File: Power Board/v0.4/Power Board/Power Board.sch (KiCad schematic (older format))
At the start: 26 parts, among them J1 Battery In, J2 JST B2PS-VH, J3 JST B2PS-VH, J4 JST B2PS-VH, J5 JST B2PS-VH, J6 JST B2PS-VH, J7 JST B2PS-VH, J9 Raspberry Pi, SW1 SW_Push

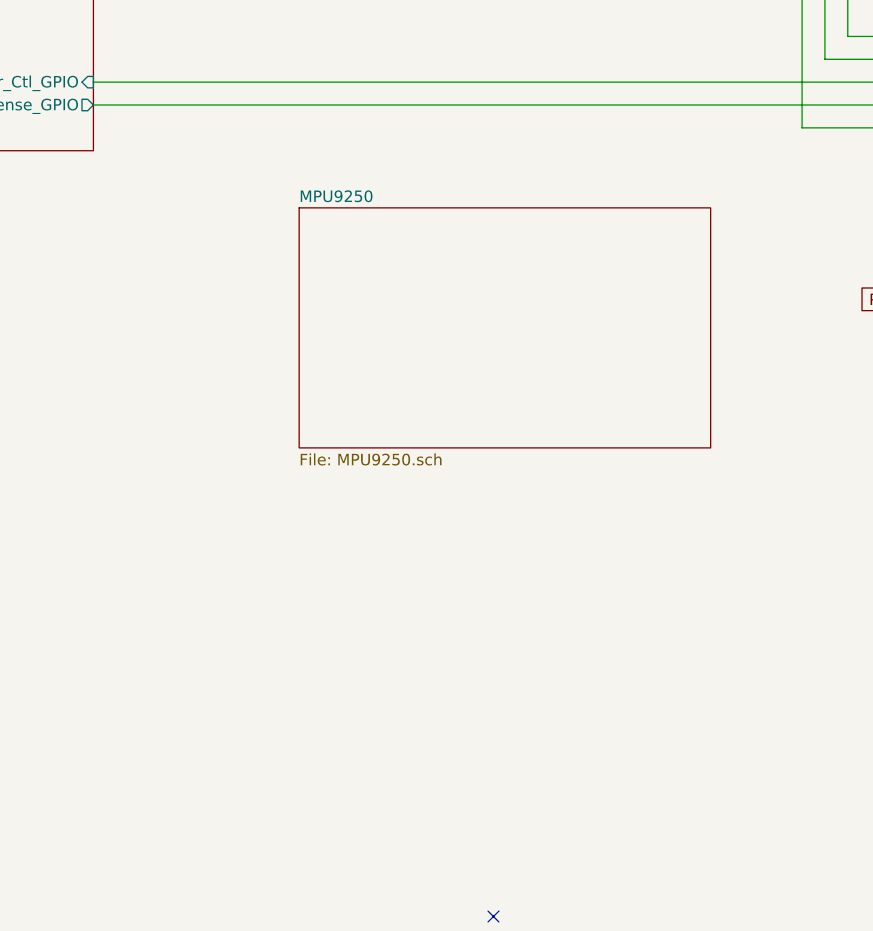
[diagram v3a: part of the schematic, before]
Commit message: Add ADC to monitor battery voltage.
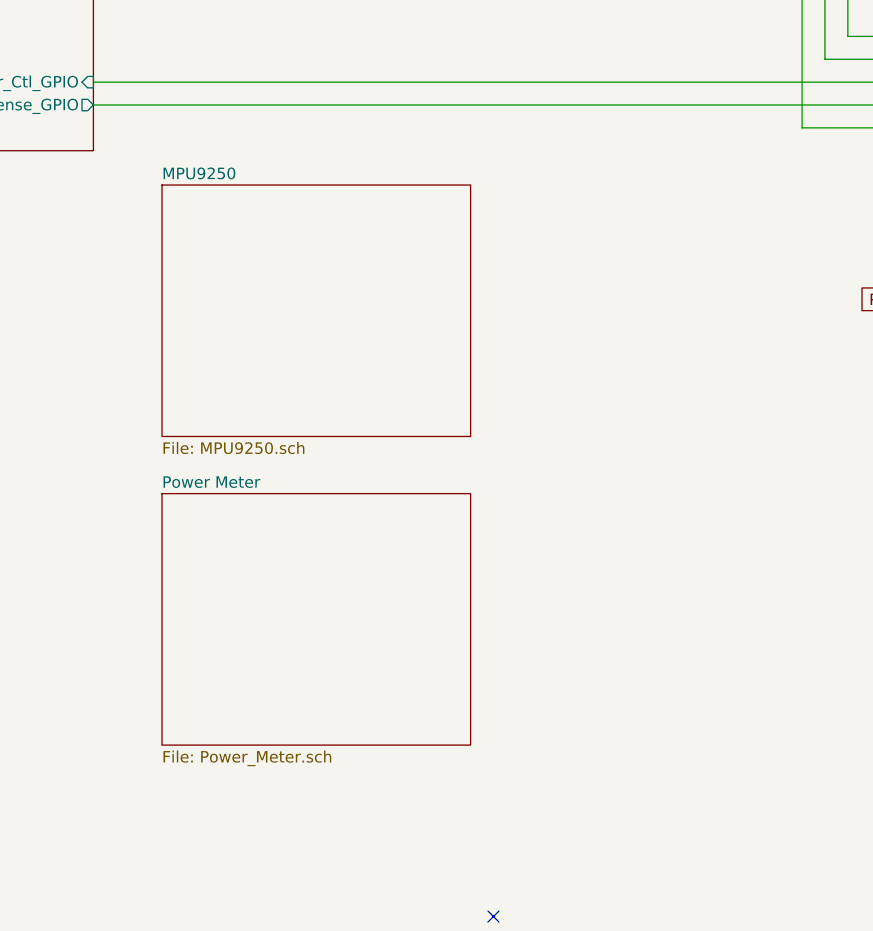
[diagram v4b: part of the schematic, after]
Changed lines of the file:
@@
 $Descr USLetter 11000 8500
 encoding utf-8
-Sheet 1 4
+Sheet 1 5
 Title "LED Cube Power Board"
 Date ""
@@
 $EndComp
 $Sheet
-S 5000 5250 1800 1050
+S 4400 5150 1350 1100
 U 5CBBBF0A
 F0 "MPU9250" 50
@@
 Wire Wire Line
 	7900 5650 8500 5650
+$Sheet
+S 4400 6500 1350 1100
+U 5CB541CC
+F0 "Power Meter" 50
+F1 "Power_Meter.sch" 50
+$EndSheet
 $EndSCHEMATC

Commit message: Almost Rough Draft Done
Mostly routed but needs lots of TLC. Need to check rule definitions before DRC
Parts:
- added R24: 100k, Resistor_SMD:R_0603_1608Metric, symbol Device:R
- L1, L2, L3, L4, L5, L6: value 70R -> 60R; footprint Inductor_SMD:L_0603_1608Metric -> Inductor_SMD:L_1206_3216Metric; Digikey No. 490-5224-1-ND -> 587-1770-1-ND; Manufacturer Murata -> Taiyo Yuden; Part No. BLM18SG700TN1D -> FBMJ3216HM600-T
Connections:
- wire segments 88 -> 89
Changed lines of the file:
@@
 $EndSheet
 Wire Wire Line
-	4900 4300 4900 2300
+	4900 4300 4900 3400
 Text Label 8850 4300 2    50   ~ 0
 +5.2V
@@
 	8300 3400 8200 3400
 $Comp
-L Device:L_Core_Ferrite_Small L6
-U 1 1 5CA7F909
-P 8400 3400
-F 0 "L6" V 8605 3400 50  0000 C CNN
-F 1 "70R" V 8514 3400 50  0000 C CNN
-F 2 "Inductor_SMD:L_0603_1608Metric" H 8400 3400 50  0001 C CNN
-F 3 "~" H 8400 3400 50  0001 C CNN
-F 4 "490-5224-1-ND" H 0   0   50  0001 C CNN "Digikey No."
-F 5 "Murata" H 0   0   50  0001 C CNN "Manufacturer"
-F 6 " BLM18SG700TN1D " H 0   0   50  0001 C CNN "Part No."
-	1    8400 3400
-	0    -1   -1   0
-$EndComp
-$Comp
-L Device:L_Core_Ferrite_Small L5
-U 1 1 5CA7EB66
-P 8400 3100
-F 0 "L5" V 8605 3100 50  0000 C CNN
-F 1 "70R" V 8514 3100 50  0000 C CNN
-F 2 "Inductor_SMD:L_0603_1608Metric" H 8400 3100 50  0001 C CNN
-F 3 "~" H 8400 3100 50  0001 C CNN
-F 4 "490-5224-1-ND" H 0   0   50  0001 C CNN "Digikey No."
-F 5 "Murata" H 0   0   50  0001 C CNN "Manufacturer"
-F 6 " BLM18SG700TN1D " H 0   0   50  0001 C CNN "Part No."
-	1    8400 3100
-	0    -1   -1   0
-$EndComp
-$Comp
-L Device:L_Core_Ferrite_Small L4
-U 1 1 5CA7DCF6
-P 8400 2800
-F 0 "L4" V 8605 2800 50  0000 C CNN
-F 1 "70R" V 8514 2800 50  0000 C CNN
-F 2 "Inductor_SMD:L_0603_1608Metric" H 8400 2800 50  0001 C CNN
-F 3 "~" H 8400 2800 50  0001 C CNN
-F 4 "490-5224-1-ND" H 0   0   50  0001 C CNN "Digikey No."
-F 5 "Murata" H 0   0   50  0001 C CNN "Manufacturer"
-F 6 " BLM18SG700TN1D " H 0   0   50  0001 C CNN "Part No."
-	1    8400 2800
-	0    -1   -1   0
-$EndComp
-$Comp
-L Device:L_Core_Ferrite_Small L3
-U 1 1 5CA7CC63
-P 8400 2500
-F 0 "L3" V 8605 2500 50  0000 C CNN
-F 1 "70R" V 8514 2500 50  0000 C CNN
-F 2 "Inductor_SMD:L_0603_1608Metric" H 8400 2500 50  0001 C CNN
-F 3 "~" H 8400 2500 50  0001 C CNN
-F 4 "490-5224-1-ND" H 0   0   50  0001 C CNN "Digikey No."
-F 5 "Murata" H 0   0   50  0001 C CNN "Manufacturer"
-F 6 " BLM18SG700TN1D " H 0   0   50  0001 C CNN "Part No."
-	1    8400 2500
-	0    -1   -1   0
-$EndComp
-$Comp
-L Device:L_Core_Ferrite_Small L2
-U 1 1 5CA7B064
-P 8400 2200
-F 0 "L2" V 8605 2200 50  0000 C CNN
-F 1 "70R" V 8514 2200 50  0000 C CNN
-F 2 "Inductor_SMD:L_0603_1608Metric" H 8400 2200 50  0001 C CNN
-F 3 "~" H 8400 2200 50  0001 C CNN
-F 4 "490-5224-1-ND" H 0   0   50  0001 C CNN "Digikey No."
-F 5 "Murata" H 0   0   50  0001 C CNN "Manufacturer"
-F 6 " BLM18SG700TN1D " H 0   0   50  0001 C CNN "Part No."
-	1    8400 2200
-	0    -1   -1   0
-$EndComp
-$Comp
 L Device:L_Core_Ferrite_Small L1
 U 1 1 5CA6BA0E
 P 8400 1900
 F 0 "L1" V 8605 1900 50  0000 C CNN
-F 1 "70R" V 8514 1900 50  0000 C CNN
-F 2 "Inductor_SMD:L_0603_1608Metric" H 8400 1900 50  0001 C CNN
-F 3 "~" H 8400 1900 50  0001 C CNN
-F 4 "490-5224-1-ND" H 0   0   50  0001 C CNN "Digikey No."
-F 5 "Murata" H 0   0   50  0001 C CNN "Manufacturer"
-F 6 " BLM18SG700TN1D " H 0   0   50  0001 C CNN "Part No."
+F 1 "60R" V 8514 1900 50  0000 C CNN
+F 2 "Inductor_SMD:L_1206_3216Metric" H 8400 1900 50  0001 C CNN
+F 3 "https://ds.yuden.co.jp/TYCOMPAS/ut/detail?pn=FBMJ3216HM600-T%20%20&u=M" H 8400 1900 50  0001 C CNN
+F 4 "587-1770-1-ND" H 0   0   50  0001 C CNN "Digikey No."
+F 5 "Taiyo Yuden" H 0   0   50  0001 C CNN "Manufacturer"
+F 6 "FBMJ3216HM600-T" H 0   0   50  0001 C CNN "Part No."
 	1    8400 1900
 	0    -1   -1   0
@@
 F1 "Power_Meter.sch" 50
 $EndSheet
+$Comp
+L Device:R R24
+U 1 1 5CC09EBC
+P 4900 3250
+F 0 "R24" H 4970 3296 50  0000 L CNN
+F 1 "100k" H 4970 3205 50  0000 L CNN
+F 2 "Resistor_SMD:R_0603_1608Metric" V 4830 3250 50  0001 C CNN
+F 3 "~" H 4900 3250 50  0001 C CNN
+	1    4900 3250
+	1    0    0    -1
+$EndComp
+Wire Wire Line
+	4900 3100 4900 2300
+$Comp
+L Device:L_Core_Ferrite_Small L2
+U 1 1 5CC32C1C
+P 8400 2200
+F 0 "L2" V 8605 2200 50  0000 C CNN
+F 1 "60R" V 8514 2200 50  0000 C CNN
+F 2 "Inductor_SMD:L_1206_3216Metric" H 8400 2200 50  0001 C CNN
+F 3 "https://ds.yuden.co.jp/TYCOMPAS/ut/detail?pn=FBMJ3216HM600-T%20%20&u=M" H 8400 2200 50  0001 C CNN
+F 4 "587-1770-1-ND" H 0   300 50  0001 C CNN "Digikey No."
+F 5 "Taiyo Yuden" H 0   300 50  0001 C CNN "Manufacturer"
+F 6 "FBMJ3216HM600-T" H 0   300 50  0001 C CNN "Part No."
+	1    8400 2200
+	0    -1   -1   0
+$EndComp
+$Comp
+L Device:L_Core_Ferrite_Small L3
+U 1 1 5CC3439F
+P 8400 2500
+F 0 "L3" V 8605 2500 50  0000 C CNN
+F 1 "60R" V 8514 2500 50  0000 C CNN
+F 2 "Inductor_SMD:L_1206_3216Metric" H 8400 2500 50  0001 C CNN
+F 3 "https://ds.yuden.co.jp/TYCOMPAS/ut/detail?pn=FBMJ3216HM600-T%20%20&u=M" H 8400 2500 50  0001 C CNN
+F 4 "587-1770-1-ND" H 0   600 50  0001 C CNN "Digikey No."
+F 5 "Taiyo Yuden" H 0   600 50  0001 C CNN "Manufacturer"
+F 6 "FBMJ3216HM600-T" H 0   600 50  0001 C CNN "Part No."
+	1    8400 2500
+	0    -1   -1   0
+$EndComp
+$Comp
+L Device:L_Core_Ferrite_Small L4
+U 1 1 5CC356E6
+P 8400 2800
+F 0 "L4" V 8605 2800 50  0000 C CNN
+F 1 "60R" V 8514 2800 50  0000 C CNN
+F 2 "Inductor_SMD:L_1206_3216Metric" H 8400 2800 50  0001 C CNN
+F 3 "https://ds.yuden.co.jp/TYCOMPAS/ut/detail?pn=FBMJ3216HM600-T%20%20&u=M" H 8400 2800 50  0001 C CNN
+F 4 "587-1770-1-ND" H 0   900 50  0001 C CNN "Digikey No."
+F 5 "Taiyo Yuden" H 0   900 50  0001 C CNN "Manufacturer"
+F 6 "FBMJ3216HM600-T" H 0   900 50  0001 C CNN "Part No."
+	1    8400 2800
+	0    -1   -1   0
+$EndComp
+$Comp
+L Device:L_Core_Ferrite_Small L5
+U 1 1 5CC3696C
+P 8400 3100
+F 0 "L5" V 8605 3100 50  0000 C CNN
+F 1 "60R" V 8514 3100 50  0000 C CNN
+F 2 "Inductor_SMD:L_1206_3216Metric" H 8400 3100 50  0001 C CNN
+F 3 "https://ds.yuden.co.jp/TYCOMPAS/ut/detail?pn=FBMJ3216HM600-T%20%20&u=M" H 8400 3100 50  0001 C CNN
+F 4 "587-1770-1-ND" H 0   1200 50  0001 C CNN "Digikey No."
+F 5 "Taiyo Yuden" H 0   1200 50  0001 C CNN "Manufacturer"
+F 6 "FBMJ3216HM600-T" H 0   1200 50  0001 C CNN "Part No."
+	1    8400 3100
+	0    -1   -1   0
+$EndComp
+$Comp
+L Device:L_Core_Ferrite_Small L6
+U 1 1 5CC38C63
+P 8400 3400
+F 0 "L6" V 8605 3400 50  0000 C CNN
+F 1 "60R" V 8514 3400 50  0000 C CNN
+F 2 "Inductor_SMD:L_1206_3216Metric" H 8400 3400 50  0001 C CNN
+F 3 "https://ds.yuden.co.jp/TYCOMPAS/ut/detail?pn=FBMJ3216HM600-T%20%20&u=M" H 8400 3400 50  0001 C CNN
+F 4 "587-1770-1-ND" H 0   1500 50  0001 C CNN "Digikey No."
+F 5 "Taiyo Yuden" H 0   1500 50  0001 C CNN "Manufacturer"
+F 6 "FBMJ3216HM600-T" H 0   1500 50  0001 C CNN "Part No."
+	1    8400 3400
+	0    -1   -1   0
+$EndComp
 $EndSCHEMATC

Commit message: More routing and zone placements. Needs more TLC Needs DRC review and fix
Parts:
- L7: value 70R -> 60R; footprint Inductor_SMD:L_0603_1608Metric -> Inductor_SMD:L_1206_3216Metric; Digikey No. 490-5224-1-ND -> 587-1770-1-ND; Manufacturer Murata -> Taiyo Yuden; Part No. BLM18SG700TN1D -> FBMJ3216HM600-T
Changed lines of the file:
@@
-$EndComp
-$Comp
-L Device:L_Core_Ferrite_Small L?
-U 1 1 5CC268DC
-P 8400 4300
-AR Path="/5C958DBD/5CC268DC" Ref="L?"  Part="1"
-AR Path="/5CC268DC" Ref="L7"  Part="1"
-F 0 "L7" V 8600 4300 50  0000 C CNN
-F 1 "70R" V 8500 4300 50  0000 C CNN
-F 2 "Inductor_SMD:L_0603_1608Metric" H 8400 4300 50  0001 C CNN
-F 3 "~" H 8400 4300 50  0001 C CNN
-F 4 "Murata" H 1150 1350 50  0001 C CNN "Manufacturer"
-F 5 " BLM18SG700TN1D " H 1150 1350 50  0001 C CNN "Part No."
-F 6 "490-5224-1-ND" H 400 0   50  0001 C CNN "Digikey No."
-	1    8400 4300
-	0    -1   -1   0
 $EndComp
 $Comp
@@
 	0    -1   -1   0
 $EndComp
+$Comp
+L Device:L_Core_Ferrite_Small L7
+U 1 1 5CC7E354
+P 8400 4300
+F 0 "L7" V 8605 4300 50  0000 C CNN
+F 1 "60R" V 8514 4300 50  0000 C CNN
+F 2 "Inductor_SMD:L_1206_3216Metric" H 8400 4300 50  0001 C CNN
+F 3 "https://ds.yuden.co.jp/TYCOMPAS/ut/detail?pn=FBMJ3216HM600-T%20%20&u=M" H 8400 4300 50  0001 C CNN
+F 4 "587-1770-1-ND" H 0   2400 50  0001 C CNN "Digikey No."
+F 5 "Taiyo Yuden" H 0   2400 50  0001 C CNN "Manufacturer"
+F 6 "FBMJ3216HM600-T" H 0   2400 50  0001 C CNN "Part No."
+	1    8400 4300
+	0    -1   -1   0
+$EndComp

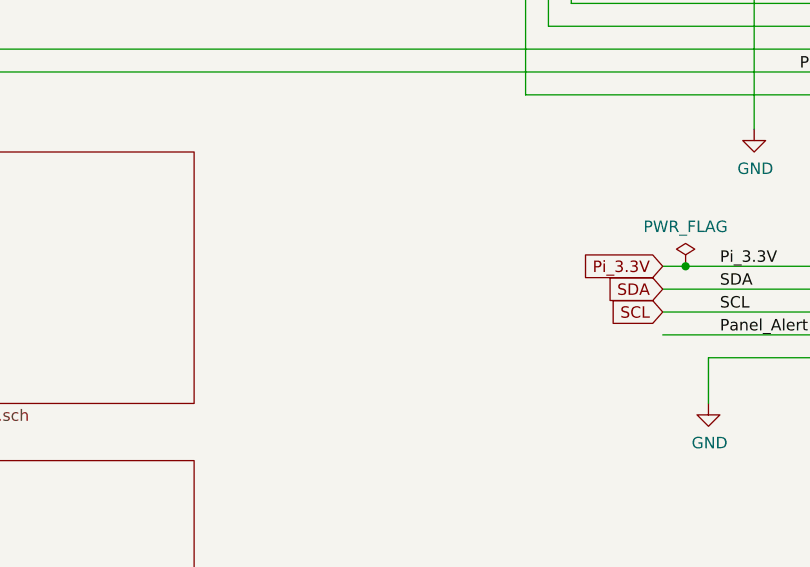
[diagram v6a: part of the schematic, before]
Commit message: Rework routing to panel connectors.  WIP.
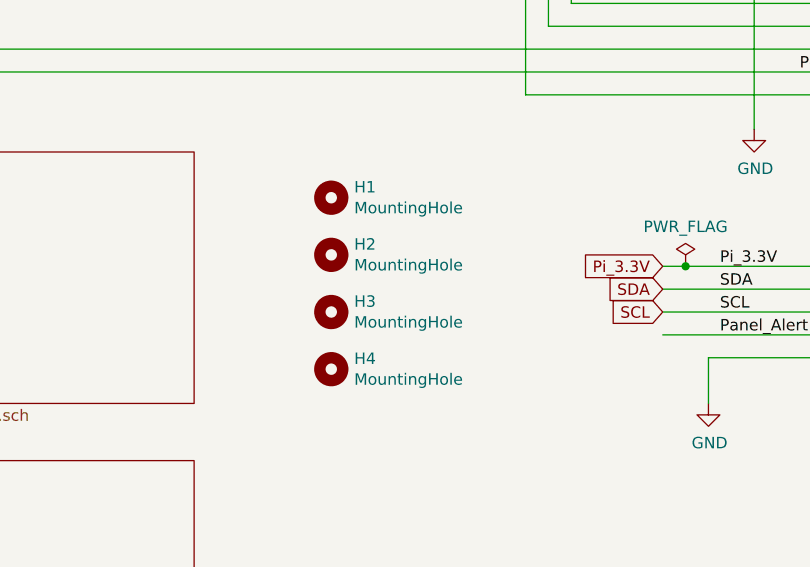
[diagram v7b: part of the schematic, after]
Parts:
- added H1, H2, H3, H4: MountingHole, MountingHole:MountingHole_2.7mm_M2.5, symbol Mechanical:MountingHole
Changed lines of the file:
@@
 	0    -1   -1   0
 $EndComp
+$Comp
+L Mechanical:MountingHole H1
+U 1 1 5CBE4232
+P 6350 5350
+F 0 "H1" H 6450 5396 50  0000 L CNN
+F 1 "MountingHole" H 6450 5305 50  0000 L CNN
+F 2 "MountingHole:MountingHole_2.7mm_M2.5" H 6350 5350 50  0001 C CNN
+F 3 "~" H 6350 5350 50  0001 C CNN
+	1    6350 5350
+	1    0    0    -1
+$EndComp
+$Comp
+L Mechanical:MountingHole H2
+U 1 1 5CBE4288
+P 6350 5600
+F 0 "H2" H 6450 5646 50  0000 L CNN
+F 1 "MountingHole" H 6450 5555 50  0000 L CNN
+F 2 "MountingHole:MountingHole_2.7mm_M2.5" H 6350 5600 50  0001 C CNN
+F 3 "~" H 6350 5600 50  0001 C CNN
+	1    6350 5600
+	1    0    0    -1
+$EndComp
+$Comp
+L Mechanical:MountingHole H3
+U 1 1 5CBE430A
+P 6350 5850
+F 0 "H3" H 6450 5896 50  0000 L CNN
+F 1 "MountingHole" H 6450 5805 50  0000 L CNN
+F 2 "MountingHole:MountingHole_2.7mm_M2.5" H 6350 5850 50  0001 C CNN
+F 3 "~" H 6350 5850 50  0001 C CNN
+	1    6350 5850
+	1    0    0    -1
+$EndComp
+$Comp
+L Mechanical:MountingHole H4
+U 1 1 5CBE438C
+P 6350 6100
+F 0 "H4" H 6450 6146 50  0000 L CNN
+F 1 "MountingHole" H 6450 6055 50  0000 L CNN
+F 2 "MountingHole:MountingHole_2.7mm_M2.5" H 6350 6100 50  0001 C CNN
+F 3 "~" H 6350 6100 50  0001 C CNN
+	1    6350 6100
+	1    0    0    -1
+$EndComp
 $EndSCHEMATC

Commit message: Add 3D models for some components.
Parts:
- J1: footprint Connector_JST:JST_VH_B3PS-VH_1x03_P3.96mm_Horizontal -> Power_Board:JST_VH_B3PS-VH_1x03_P3.96mm_Horizontal
- J2, J3, J4, J5, J6, J7: footprint Connector_JST:JST_VH_B2PS-VH_1x02_P3.96mm_Horizontal -> Power_Board:JST_VH_B2PS-VH_1x02_P3.96mm_Horizontal
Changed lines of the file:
@@
 F 0 "J7" H 9130 3392 50  0000 L CNN
 F 1 "JST B2PS-VH" H 9130 3301 50  0000 L CNN
-F 2 "Connector_JST:JST_VH_B2PS-VH_1x02_P3.96mm_Horizontal" H 9050 3400 50  0001 C CNN
+F 2 "Power_Board:JST_VH_B2PS-VH_1x02_P3.96mm_Horizontal" H 9050 3400 50  0001 C CNN
 F 3 "~" H 9050 3400 50  0001 C CNN
 F 4 "455-1648-ND" H -50 1950 50  0001 C CNN "Digikey No."
@@
 F 0 "J6" H 9130 3092 50  0000 L CNN
 F 1 "JST B2PS-VH" H 9130 3001 50  0000 L CNN
-F 2 "Connector_JST:JST_VH_B2PS-VH_1x02_P3.96mm_Horizontal" H 9050 3100 50  0001 C CNN
+F 2 "Power_Board:JST_VH_B2PS-VH_1x02_P3.96mm_Horizontal" H 9050 3100 50  0001 C CNN
 F 3 "~" H 9050 3100 50  0001 C CNN
 F 4 "455-1648-ND" H -50 1650 50  0001 C CNN "Digikey No."
@@
 F 0 "J5" H 9130 2792 50  0000 L CNN
 F 1 "JST B2PS-VH" H 9130 2701 50  0000 L CNN
-F 2 "Connector_JST:JST_VH_B2PS-VH_1x02_P3.96mm_Horizontal" H 9050 2800 50  0001 C CNN
+F 2 "Power_Board:JST_VH_B2PS-VH_1x02_P3.96mm_Horizontal" H 9050 2800 50  0001 C CNN
 F 3 "~" H 9050 2800 50  0001 C CNN
 F 4 "455-1648-ND" H -50 1350 50  0001 C CNN "Digikey No."
@@
 F 0 "J4" H 9130 2492 50  0000 L CNN
 F 1 "JST B2PS-VH" H 9130 2401 50  0000 L CNN
-F 2 "Connector_JST:JST_VH_B2PS-VH_1x02_P3.96mm_Horizontal" H 9050 2500 50  0001 C CNN
+F 2 "Power_Board:JST_VH_B2PS-VH_1x02_P3.96mm_Horizontal" H 9050 2500 50  0001 C CNN
 F 3 "~" H 9050 2500 50  0001 C CNN
 F 4 "455-1648-ND" H -50 1050 50  0001 C CNN "Digikey No."
@@
 F 0 "J3" H 9130 2192 50  0000 L CNN
 F 1 "JST B2PS-VH" H 9130 2101 50  0000 L CNN
-F 2 "Connector_JST:JST_VH_B2PS-VH_1x02_P3.96mm_Horizontal" H 9050 2200 50  0001 C CNN
+F 2 "Power_Board:JST_VH_B2PS-VH_1x02_P3.96mm_Horizontal" H 9050 2200 50  0001 C CNN
 F 3 "~" H 9050 2200 50  0001 C CNN
 F 4 "455-1648-ND" H -50 750 50  0001 C CNN "Digikey No."
@@
 F 0 "J2" H 9130 1892 50  0000 L CNN
 F 1 "JST B2PS-VH" H 9130 1801 50  0000 L CNN
-F 2 "Connector_JST:JST_VH_B2PS-VH_1x02_P3.96mm_Horizontal" H 9050 1900 50  0001 C CNN
+F 2 "Power_Board:JST_VH_B2PS-VH_1x02_P3.96mm_Horizontal" H 9050 1900 50  0001 C CNN
 F 3 "~" H 9050 1900 50  0001 C CNN
 F 4 "455-1648-ND" H -50 450 50  0001 C CNN "Digikey No."
@@
 F 0 "J1" H 992 2185 50  0000 C CNN
 F 1 "Battery In" H 992 2094 50  0000 C CNN
-F 2 "Connector_JST:JST_VH_B3PS-VH_1x03_P3.96mm_Horizontal" H 1100 2000 50  0001 C CNN
+F 2 "Power_Board:JST_VH_B3PS-VH_1x03_P3.96mm_Horizontal" H 1100 2000 50  0001 C CNN
 F 3 "https://www.molex.com/pdm_docs/sd/436500205_sd.pdf" H 1100 2000 50  0001 C CNN
 F 4 "WM17581-ND" H -650 -750 50  0001 C CNN "Digikey No."
